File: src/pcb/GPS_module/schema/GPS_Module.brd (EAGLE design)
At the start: 23.8 x 25.4 mm, 6 parts, among them U1 SL876Q5A001T001000

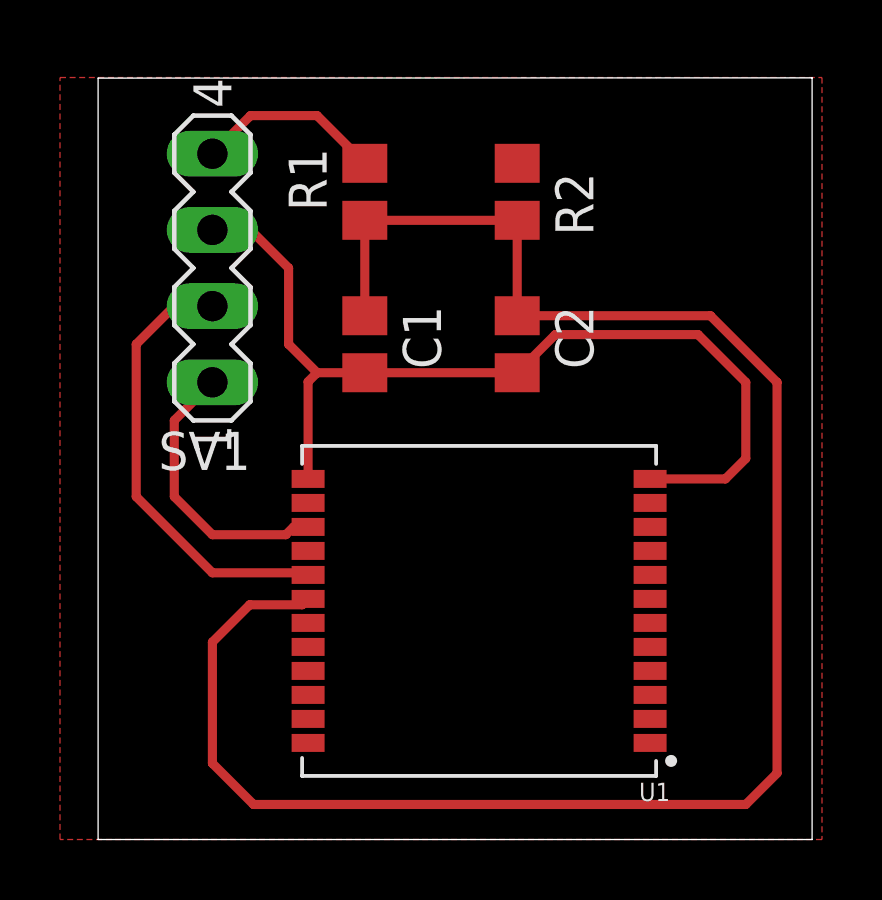
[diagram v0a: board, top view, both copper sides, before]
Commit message: added humidity sensor scheme, board scheme, images and updated GPS module
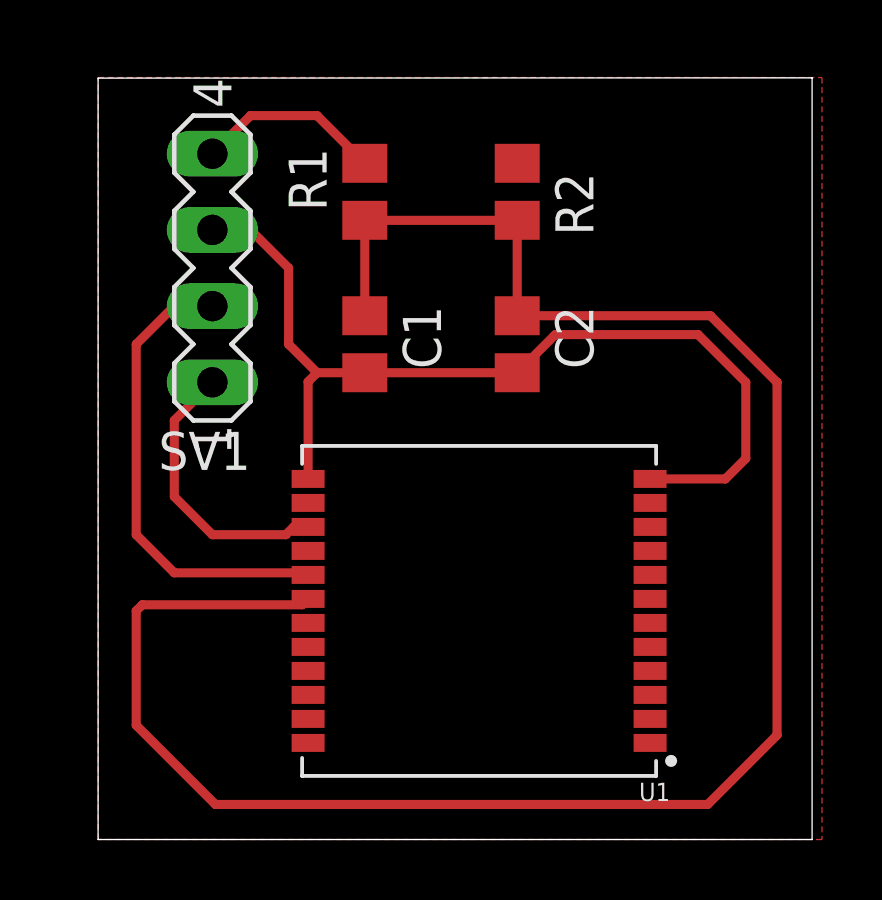
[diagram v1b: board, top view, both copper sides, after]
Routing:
- net VIN: track 61.7 -> 65.9 mm
- net TX: track 15.0 -> 15.7 mm
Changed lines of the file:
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@@
 <layer number="43" name="vRestrict" color="2" fill="10" visible="yes" active="yes"/>
 <layer number="44" name="Drills" color="7" fill="1" visible="no" active="yes"/>
-<layer number="45" name="Holes" color="7" fill="1" visible="no" active="yes"/>
+<layer number="45" name="Holes" color="7" fill="1" visible="yes" active="yes"/>
 <layer number="46" name="Milling" color="3" fill="1" visible="no" active="yes"/>
 <layer number="47" name="Measures" color="7" fill="1" visible="no" active="yes"/>
@@
 <layer number="97" name="Info" color="7" fill="1" visible="no" active="no"/>
 <layer number="98" name="Guide" color="6" fill="1" visible="no" active="no"/>
+<layer number="99" name="SpiceOrder" color="7" fill="1" visible="no" active="no"/>
 </layers>
 <board>
-<fusionsync huburn="a.YnVzaW5lc3M6aG90bWFpbDY1Mzg5" projecturn="a.YnVzaW5lc3M6aG90bWFpbDY1Mzg5I0QyMDE5MDkyODIyMDA1ODM3Ng" f3durn="urn:adsk.wipprod:dm.lineage:KzSlArEYRVO6wvjfa0oVZg" pcbguid="ebf4a580-fadc-4f0f-b7d8-5e078fd26f8d" lastpulledtime="" lastsyncedchangeguid="86477c8c-2dbf-6ea0-a334-8467ebd24e8b"/>
+<fusionsync huburn="a.YnVzaW5lc3M6aG90bWFpbDY1Mzg5" projecturn="a.YnVzaW5lc3M6aG90bWFpbDY1Mzg5I0QyMDE5MDkyODIyMDA1ODM3Ng" f3durn="urn:adsk.wipprod:dm.lineage:KzSlArEYRVO6wvjfa0oVZg" pcbguid="ebf4a580-fadc-4f0f-b7d8-5e078fd26f8d" lastpulledtime="" lastsyncedchangeguid="bdface93-1f0a-7969-1048-1f6c891c56d1"/>
 <plain>
 <wire x1="23.8" y1="10.16" x2="23.8" y2="35.55" width="0" layer="20"/>
@@
 <wire x1="3.81" y1="27.94" x2="2.54" y2="27.94" width="0.3048" layer="1"/>
 <wire x1="2.54" y1="27.94" x2="1.27" y2="26.67" width="0.3048" layer="1"/>
-<wire x1="1.27" y1="26.67" x2="1.27" y2="21.59" width="0.3048" layer="1"/>
-<wire x1="1.27" y1="21.59" x2="3.81" y2="19.05" width="0.3048" layer="1"/>
+<wire x1="1.27" y1="26.67" x2="1.27" y2="20.32" width="0.3048" layer="1"/>
+<wire x1="1.27" y1="20.32" x2="2.54" y2="19.05" width="0.3048" layer="1"/>
 <wire x1="6.93" y1="19.05" x2="7" y2="18.98" width="0.3048" layer="1"/>
-<wire x1="3.81" y1="19.05" x2="6.93" y2="19.05" width="0.3048" layer="1"/>
+<wire x1="2.54" y1="19.05" x2="6.93" y2="19.05" width="0.3048" layer="1"/>
 </signal>
 <signal name="GND">
@@
 <wire x1="7" y1="25.42" x2="7.3" y2="25.72" width="0.3048" layer="1"/>
 <polygon width="0.1524" layer="1">
-<vertex x="-1.27" y="35.56"/>
+<vertex x="0" y="35.56"/>
 <vertex x="24.13" y="35.56"/>
 <vertex x="24.13" y="10.16"/>
-<vertex x="-1.27" y="10.16"/>
+<vertex x="0" y="10.16"/>
 </polygon>
-<wire x1="13.97" y1="25.72" x2="13.97" y2="32.7" width="0" layer="19" extent="1-1"/>
-<wire x1="18.4" y1="20.58" x2="18.4" y2="22.18" width="0" layer="19" extent="1-1"/>
-<wire x1="18.4" y1="16.58" x2="18.4" y2="20.58" width="0" layer="19" extent="1-1"/>
-<wire x1="18.4" y1="14.98" x2="18.4" y2="16.58" width="0" layer="19" extent="1-1"/>
-<wire x1="18.4" y1="14.18" x2="18.4" y2="14.98" width="0" layer="19" extent="1-1"/>
-<wire x1="7" y1="16.58" x2="7" y2="22.18" width="0" layer="19" extent="1-1"/>
-<wire x1="7" y1="13.38" x2="7" y2="16.58" width="0" layer="19" extent="1-1"/>
 </signal>
 <signal name="VDD">
@@
 <wire x1="13.97" y1="27.62" x2="20.4116" y2="27.62" width="0.3048" layer="1"/>
 <wire x1="20.4116" y1="27.62" x2="22.6316" y2="25.4" width="0.3048" layer="1"/>
-<wire x1="22.6316" y1="25.4" x2="22.6316" y2="12.37" width="0.3048" layer="1"/>
-<wire x1="22.6316" y1="12.37" x2="21.59" y2="11.3284" width="0.3048" layer="1"/>
-<wire x1="21.59" y1="11.3284" x2="5.1816" y2="11.3284" width="0.3048" layer="1"/>
-<wire x1="5.05375" y1="17.9848" x2="6.8048" y2="17.9848" width="0.3048" layer="1"/>
+<wire x1="22.6316" y1="25.4" x2="22.6316" y2="13.64" width="0.3048" layer="1"/>
+<wire x1="22.6316" y1="13.64" x2="20.32" y2="11.3284" width="0.3048" layer="1"/>
+<wire x1="20.32" y1="11.3284" x2="3.9116" y2="11.3284" width="0.3048" layer="1"/>
+<wire x1="1.27" y1="13.97" x2="1.27" y2="17.78" width="0.3048" layer="1"/>
+<wire x1="1.27" y1="17.78" x2="1.4748" y2="17.9848" width="0.3048" layer="1"/>
+<wire x1="1.4748" y1="17.9848" x2="6.8048" y2="17.9848" width="0.3048" layer="1"/>
 <wire x1="6.8048" y1="17.9848" x2="7" y2="18.18" width="0.3048" layer="1"/>
-<wire x1="3.81" y1="16.74105" x2="5.05375" y2="17.9848" width="0.3048" layer="1"/>
-<wire x1="5.1816" y1="11.3284" x2="3.81" y2="12.7" width="0.3048" layer="1"/>
-<wire x1="3.81" y1="12.7" x2="3.81" y2="16.74105" width="0.3048" layer="1"/>
+<wire x1="3.9116" y1="11.3284" x2="1.27" y2="13.97" width="0.3048" layer="1"/>
 </signal>
 <signal name="RX">

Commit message: updated footprint, humidity sensor pcb, gps module pcb and images, added gerberfiles
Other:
- outline, holes or cut-outs redrawn
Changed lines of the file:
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@@
 </layers>
 <board>
-<fusionsync huburn="a.YnVzaW5lc3M6aG90bWFpbDY1Mzg5" projecturn="a.YnVzaW5lc3M6aG90bWFpbDY1Mzg5I0QyMDE5MDkyODIyMDA1ODM3Ng" f3durn="urn:adsk.wipprod:dm.lineage:KzSlArEYRVO6wvjfa0oVZg" pcbguid="ebf4a580-fadc-4f0f-b7d8-5e078fd26f8d" lastpulledtime="" lastsyncedchangeguid="bdface93-1f0a-7969-1048-1f6c891c56d1"/>
+<fusionsync huburn="a.YnVzaW5lc3M6aG90bWFpbDY1Mzg5" projecturn="a.YnVzaW5lc3M6aG90bWFpbDY1Mzg5I0QyMDE5MDkyODIyMDA1ODM3Ng" f3durn="urn:adsk.wipprod:dm.lineage:KzSlArEYRVO6wvjfa0oVZg" pcbguid="ebf4a580-fadc-4f0f-b7d8-5e078fd26f8d" lastpulledtime="" lastsyncedchangeguid="33841908-6723-2d42-ed1a-ce92a6612f6a"/>
 <plain>
-<wire x1="23.8" y1="10.16" x2="23.8" y2="35.55" width="0" layer="20"/>
-<wire x1="23.8" y1="35.55" x2="0" y2="35.539840625" width="0" layer="20"/>
-<wire x1="0" y1="35.539840625" x2="0" y2="10.16" width="0" layer="20"/>
-<wire x1="0" y1="10.16" x2="23.8" y2="10.16" width="0" layer="20"/>
-<dimension x1="0" y1="35.539840625" x2="23.8" y2="35.55" x3="11.899453125" y3="36.82531875" textsize="1.778" layer="1"/>
-<dimension x1="0" y1="35.539840625" x2="0" y2="10.16" x3="-1.27" y3="22.84991875" textsize="1.778" layer="1"/>
+<wire x1="3.81" y1="10.16" x2="20.32" y2="10.16" width="0" layer="20"/>
+<wire x1="20.32" y1="10.16" x2="23.8" y2="13.64" width="0" layer="20"/>
+<wire x1="23.8" y1="13.64" x2="23.8" y2="27.00203125" width="0" layer="20"/>
+<wire x1="23.8" y1="27.00203125" x2="15.25203125" y2="35.54635" width="0" layer="20"/>
+<wire x1="15.25203125" y1="35.54635" x2="0" y2="35.539840625" width="0" layer="20"/>
+<wire x1="0" y1="35.539840625" x2="0" y2="13.97" width="0" layer="20"/>
+<wire x1="0" y1="13.97" x2="3.81" y2="10.16" width="0" layer="20"/>
 </plain>
 <attributes>
@@
 </class>
 </classes>
-<designrules name="default">
+<designrules name="default *">
 <description language="de">&lt;b&gt;EAGLE Design Rules&lt;/b&gt;
 &lt;p&gt;
@@
 <param name="mdViaViaSameLayer" value="6mil"/>
 <param name="mnLayersViaInSmd" value="2"/>
-<param name="mdCopperDimension" value="40mil"/>
+<param name="mdCopperDimension" value="0mil"/>
 <param name="mdDrill" value="6mil"/>
 <param name="mdSmdStop" value="0mil"/>
@@
 <polygon width="0.1524" layer="1">
 <vertex x="0" y="35.56"/>
-<vertex x="24.13" y="35.56"/>
-<vertex x="24.13" y="10.16"/>
-<vertex x="0" y="10.16"/>
+<vertex x="15.24" y="35.56"/>
+<vertex x="24.13" y="26.67"/>
+<vertex x="24.13" y="13.97"/>
+<vertex x="20.32" y="10.16"/>
+<vertex x="3.81" y="10.16"/>
+<vertex x="0" y="13.97"/>
 </polygon>
 </signal>
